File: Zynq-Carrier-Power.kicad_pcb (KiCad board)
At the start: 2 copper layers, 49 x 41 mm, 33 parts, among them J1 Zynq_SoM, J10 Barrel_Jack_MountingPin, J2 B2B-PH-K-S, J3 USB_C_Receptacle_USB2.0_16P, J4 Conn_01x03, J5 Conn_01x03, J6 Conn_01x03, J7 Conn_01x02, J8 Conn_01x02, J9 Conn_01x03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

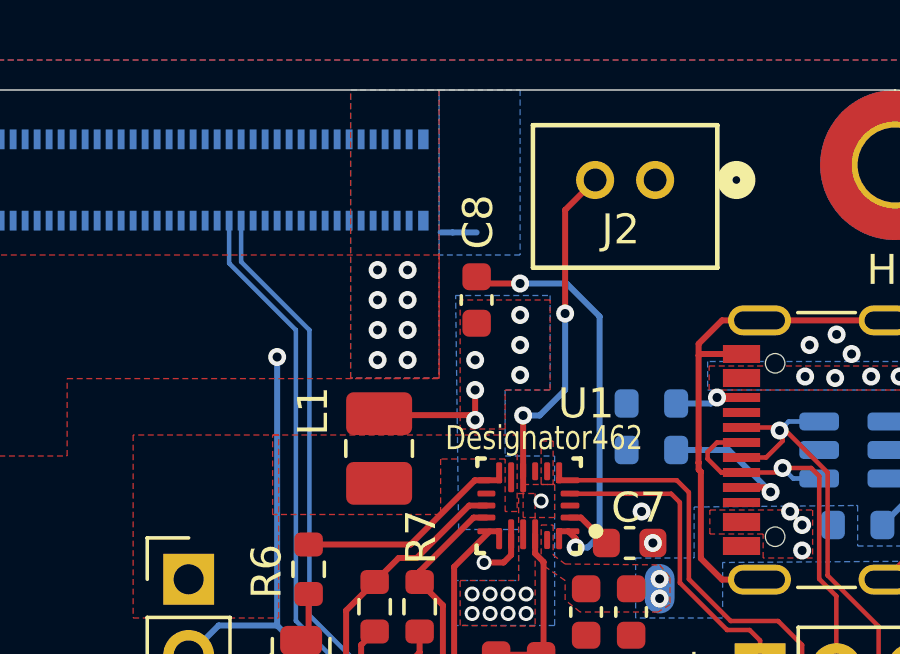
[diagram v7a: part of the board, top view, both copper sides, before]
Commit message: Fixed Final Errors
Only errors left are small thermal relief issues that are a part of the zynq carrier footprint.
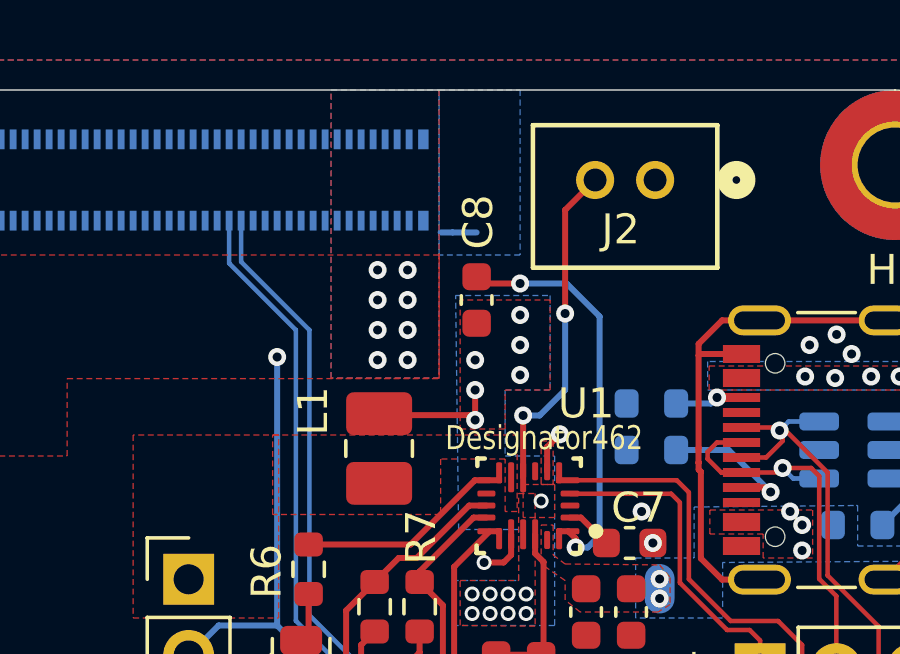
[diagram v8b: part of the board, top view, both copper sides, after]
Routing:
- net GND: track 30.3 -> 31.7 mm, vias 16 -> 17
